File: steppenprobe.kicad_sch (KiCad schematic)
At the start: 85 parts, among them J1 USB_C_Receptacle_USB2.0, J2 Conn_ST_STDC14, J4 Conn_01x16, Q1 2N7002, SW1 SW_SPDT, SW2 SW_Push, U1 FT2232HL, U10 74LVC1G125, U11 74LVC1G125, U12 74LVC1G125, U2 XC6206PxxxMR, U3 SRV05-4, U4 93LCxxB, U5 74LVC1G125, U6 74LVC1G126, U7 74LVC1G125, U8 74LVC1G125, U9 74LVC1G125, Y1 Crystal_GND24

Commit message: Removed EEPROM.
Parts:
- removed C18: 100nF, Capacitor_SMD:C_0603_1608Metric, symbol Device:C
- removed R3: 10k, Resistor_SMD:R_0603_1608Metric, symbol Device:R
- removed R5: 2k, Resistor_SMD:R_0603_1608Metric, symbol Device:R
- removed U4: 93LCxxB, Package_SO:SOIC-8_3.9x4.9mm_P1.27mm, symbol Memory_EEPROM:93LCxxB
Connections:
- net EE_CLK: no longer names the net of U1.62 (EECLK)
- net EE_CS: no longer names the net of U1.63 (EECS)
- net EE_DATA: no longer names the net of U1.61 (EEDATA)
- no-connect marks 18 -> 21
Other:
- note removed: "EEPROM (optional)"
- company: Diego Herranz -> Ondrej Golasowski
- title: Steppenprobe -> vesp-jtag

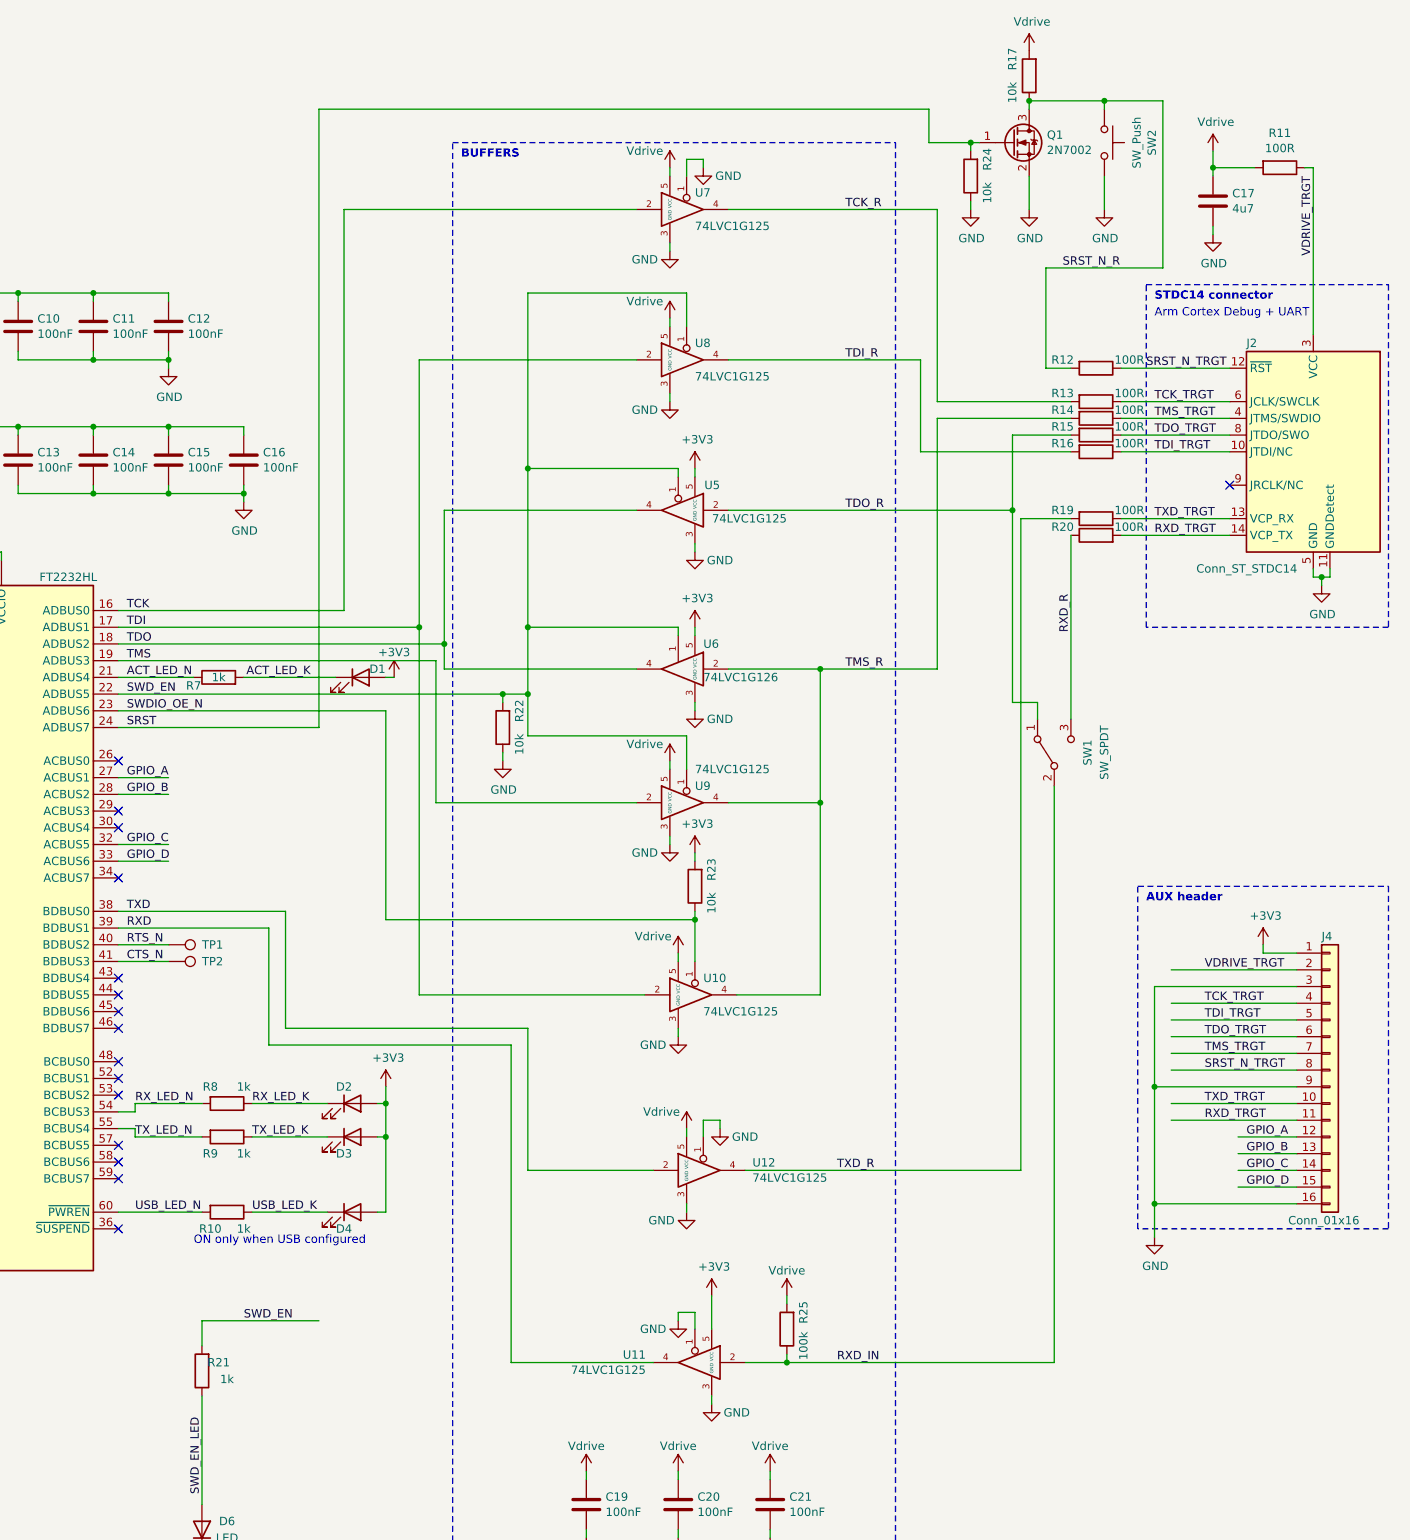
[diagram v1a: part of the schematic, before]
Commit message: Added PMOD.
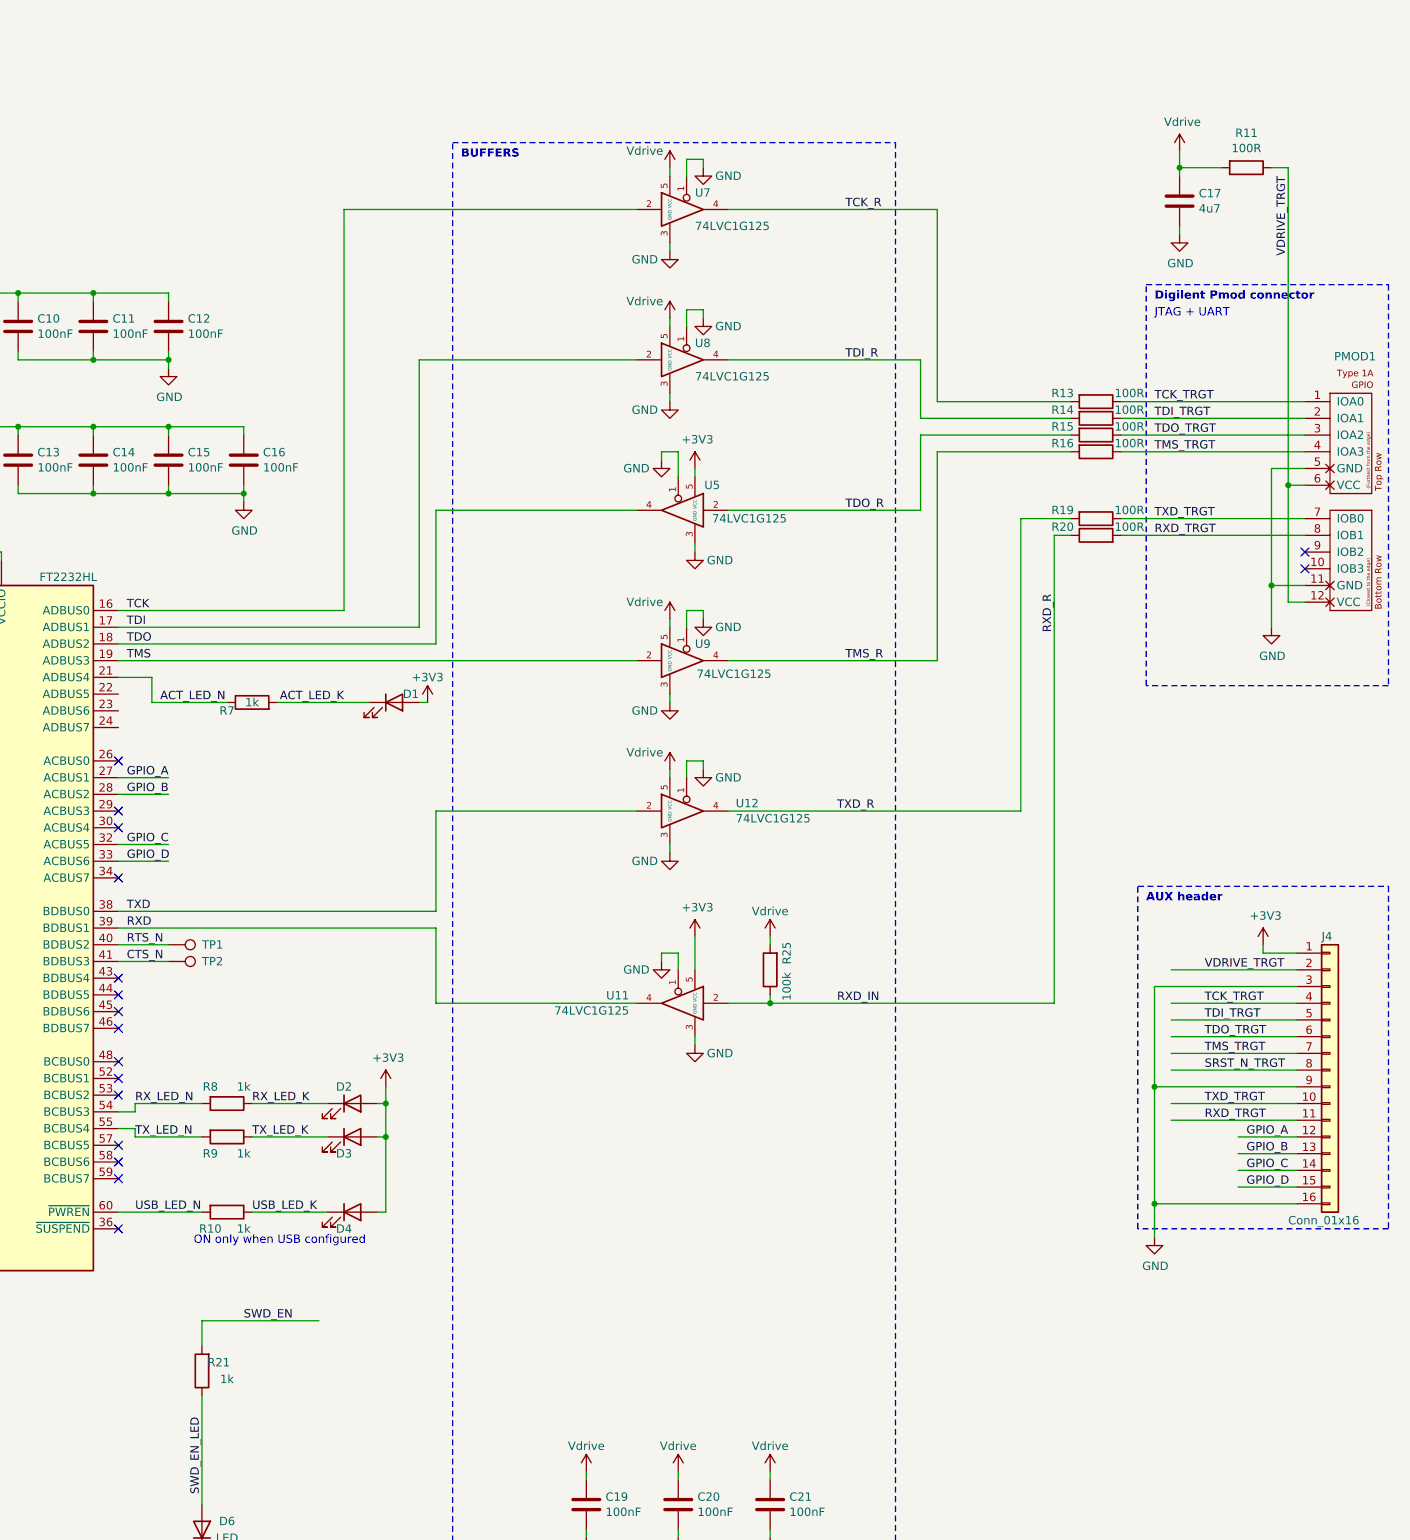
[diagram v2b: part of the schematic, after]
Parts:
- removed J2: Conn_ST_STDC14, Connector_PinHeader_1.27mm:PinHeader_2x07_P1.27mm_Vertical_SMD, symbol Connector:Conn_ST_STDC14
- removed Q1: 2N7002, Package_TO_SOT_SMD:SOT-23, symbol Transistor_FET:2N7002
- removed R12: 100R, Resistor_SMD:R_0603_1608Metric, symbol Device:R
- removed R17, R22, R23, R24: 10k, Resistor_SMD:R_0603_1608Metric, symbol Device:R
- removed SW1: SW_SPDT, Button_Switch_SMD:SW_SPDT_PCM12, symbol Switch:SW_SPDT
- removed SW2: SW_Push, Button_Switch_SMD:SW_Push_1P1T_NO_E-Switch_TL3301NxxxxxG, symbol Switch:SW_Push
- removed U10: 74LVC1G125, Package_TO_SOT_SMD:SOT-353_SC-70-5, symbol 74xxGxx_power_pins:74LVC1G125-74xGxx
- removed U6: 74LVC1G126, Package_TO_SOT_SMD:SOT-353_SC-70-5, symbol 74xxGxx_power_pins:74LVC1G126-74xGxx
- added PMOD1: PMOD-Device-x2-Type-1A-GPIO, pmod-conn_6x2:pmod_pin_array_6x2, symbol PMOD:PMOD-Device-x2-Type-1A-GPIO
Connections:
- net RXD_R is gone; now on net RXD_IN: R20.1
- net GND: now also U5.1, U8.1, U9.1, PMOD1.11 (GND), PMOD1.5 (GND)
- net RXD_TRGT: now also PMOD1.8 (IOB1)
- net SWD_EN: no longer U1.22 (ADBUS5), U5.1, U8.1, U9.1
- net TCK_TRGT: now also PMOD1.1 (IOA0)
- net TDI_R: now also R14.2; no longer R16.2
- net TDI_TRGT: now also R14.1, PMOD1.2 (IOA1); no longer R16.1
- net TDO_TRGT: now also PMOD1.3 (IOA2)
- net TMS_R: now also R16.2; no longer R14.2
- net TMS_TRGT: now also R16.1, PMOD1.4 (IOA3); no longer R14.1
- net TXD_TRGT: now also PMOD1.7 (IOB0)
- net VDRIVE_TRGT: now also PMOD1.12 (VCC), PMOD1.6 (VCC)
- net SRST: no longer names the net of U1.24 (ADBUS7)
- net SWDIO_OE_N: no longer names the net of U1.23 (ADBUS6)
- no-connect marks 21 -> 22
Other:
- note added: "Digilent Pmod connector"
- note added: "JTAG + UART"
- note removed: "Arm Cortex Debug + UART"
- note removed: "STDC14 connector"
- moved on the sheet: C17, D1, R11, R25, R7, U11, U12, U9

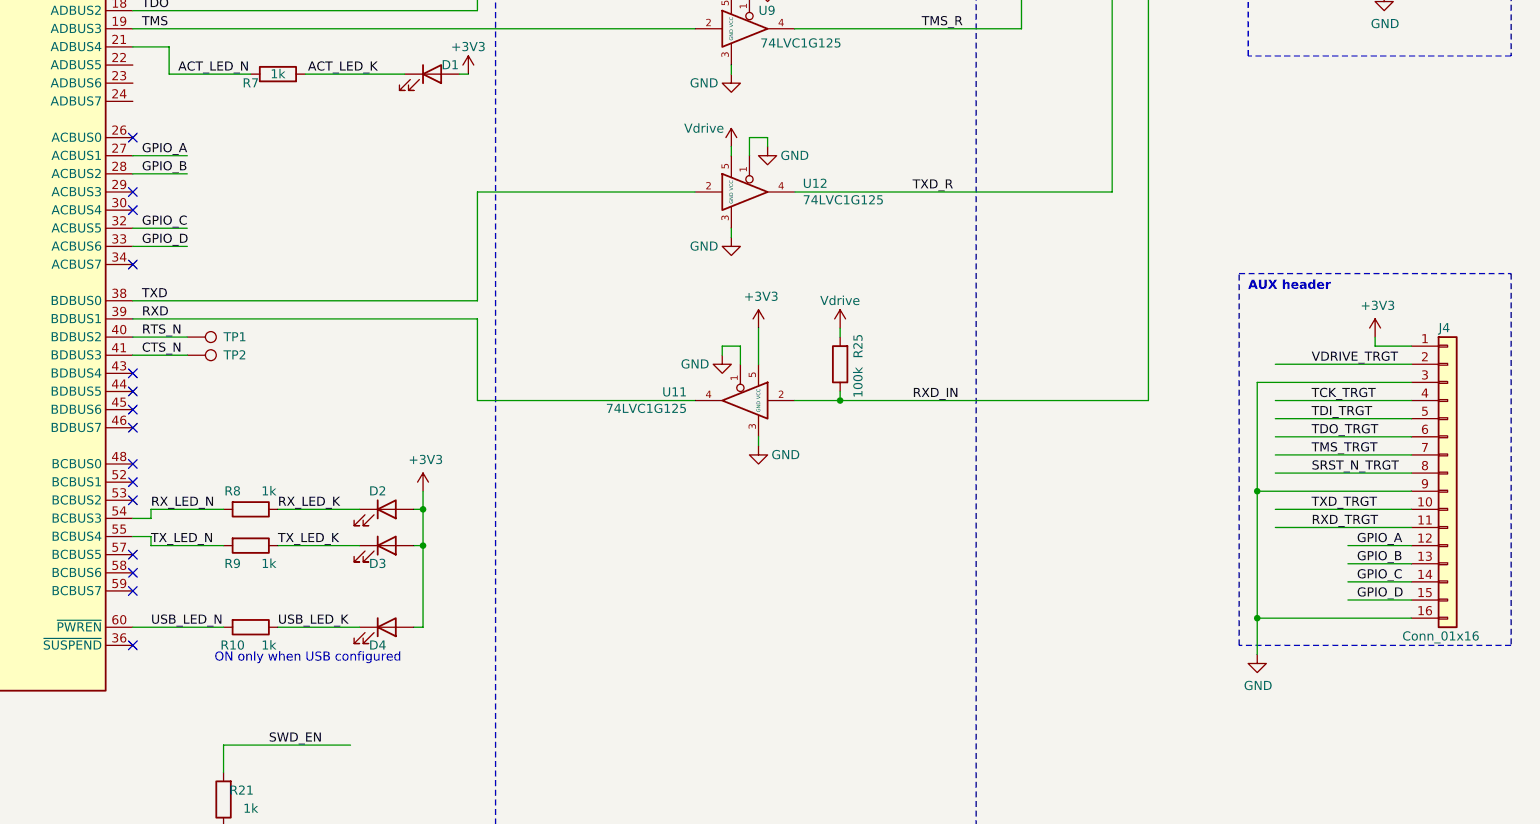
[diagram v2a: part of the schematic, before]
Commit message: Added user leds, removed uneccessary connections.
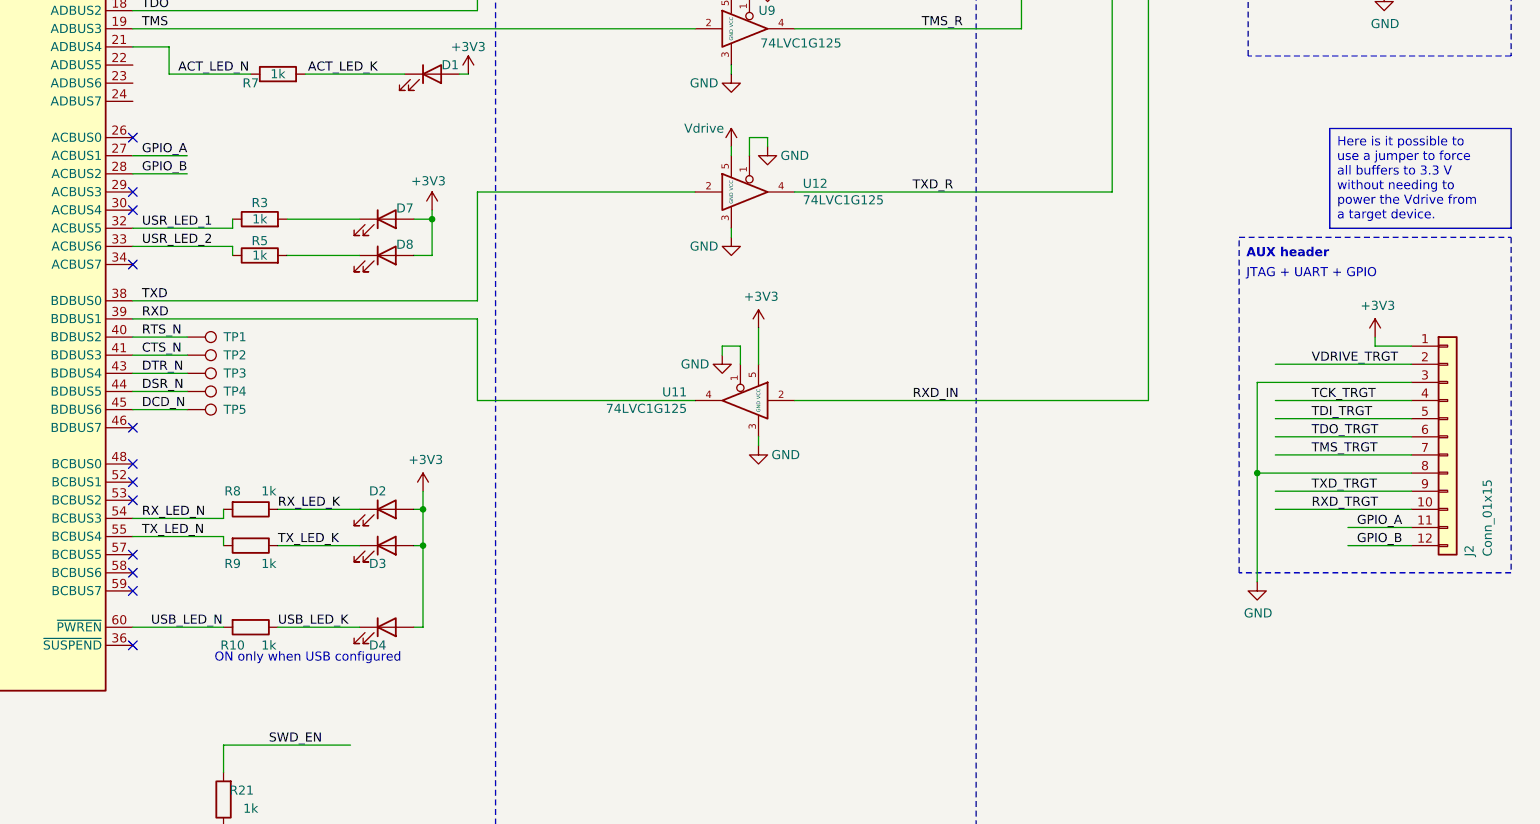
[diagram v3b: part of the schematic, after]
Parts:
- removed J4: Conn_01x16, Connector_PinHeader_2.54mm:PinHeader_1x16_P2.54mm_Vertical, symbol Connector_Generic:Conn_01x16
- removed R25: 100k, Resistor_SMD:R_0603_1608Metric, symbol Device:R
- added D7, D8: LED, symbol Device:LED
- added J2: Conn_01x15, symbol Connector_Generic:Conn_01x12
- added R3, R5: 1k, symbol Device:R
- added TP3, TP4, TP5: TestPoint, symbol Connector:TestPoint
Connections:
- net +3V3: now also D7.2 (A), D8.2 (A), J2.1 (Pin_1)
- net GND: now also J2.3 (Pin_3), J2.8 (Pin_8)
- net GPIO_A: now also J2.11 (Pin_11)
- net GPIO_B: now also J2.12 (Pin_12)
- net RXD_TRGT: now also J2.10 (Pin_10)
- net TCK_TRGT: now also J2.4 (Pin_4)
- net TDI_TRGT: now also J2.5 (Pin_5)
- net TDO_TRGT: now also J2.6 (Pin_6)
- net TMS_TRGT: now also J2.7 (Pin_7)
- net TXD_TRGT: now also J2.9 (Pin_9)
- net VDRIVE_TRGT: now also J2.2 (Pin_2)
- net DTR_N: now reaches U1.43 (BDBUS4)
- net DTR_N: now also TP3.1
- net DSR_N: now reaches U1.44 (BDBUS5)
- net DSR_N: now also TP4.1
- net DCD_N: now reaches U1.45 (BDBUS6)
- net DCD_N: now also TP5.1
- net GPIO_C renamed USR_LED_1
- net USR_LED_1: now also R3.1
- net GPIO_D renamed USR_LED_2
- net USR_LED_2: now also R5.1
- new net: D8.1 (K), R5.2
- new net: D7.1 (K), R3.2
- no-connect marks 22 -> 19
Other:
- note added: "JTAG + UART + GPIO"

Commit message: Fixed errors, assigned footprints.
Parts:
- removed D6: LED, LED_SMD:LED_0603_1608Metric, symbol Device:LED
- removed R21: 1k, Resistor_SMD:R_0603_1608Metric, symbol Device:R
- D7, D8: footprint (none) -> LED_SMD:LED_0603_1608Metric
- FB1, FB2, FB3: symbol Device:Ferrite_Bead -> Device:FerriteBead
- J1: symbol Connector:USB_C_Receptacle_USB2.0 -> Connector:USB_C_Receptacle_USB2.0_14P
- J2: value Conn_01x15 -> Conn_01x12; footprint (none) -> Connector_PinHeader_2.54mm:PinHeader_1x12_P2.54mm_Vertical
- R3: footprint (none) -> Resistor_SMD:R_0603_1608Metric
- R5: footprint (none) -> Resistor_SMD:R_1206_3216Metric
- TP3, TP4, TP5: footprint (none) -> TestPoint:TestPoint_Pad_D1.0mm
- U2: footprint Package_TO_SOT_SMD:SOT-23 -> Package_TO_SOT_SMD:SOT-23-3
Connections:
- net RXD_IN renamed RXD_R
- no-connect marks 19 -> 20
